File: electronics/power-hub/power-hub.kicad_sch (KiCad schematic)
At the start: 0 parts

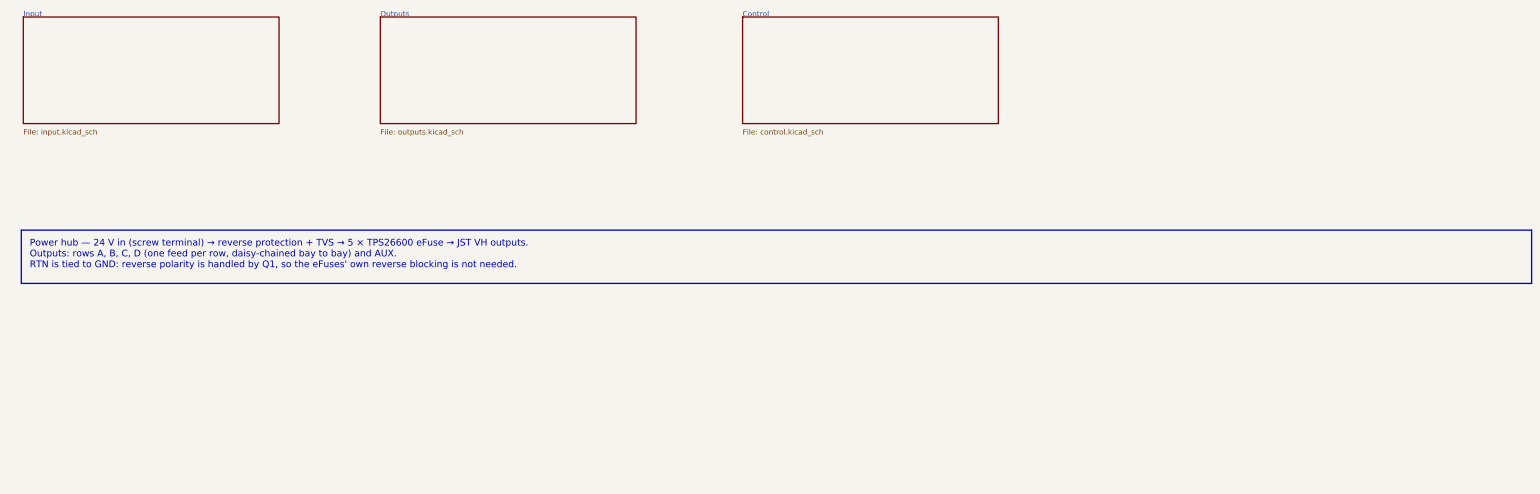
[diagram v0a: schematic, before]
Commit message: Schematics: draw real wires and an overview block diagram
The generator used to connect every pin through a net label only. Now,
in each block, the part with the most pins is the anchor and the
two-pin parts that share a signal with one of its side pins hang off
that pin on a real wire; parts chained behind them (R -> C -> GND)
stack underneath, and anchor-less blocks (pull-ups, reset/boot
buttons) are adopted by the anchor they connect to. Power symbols on
side pins point outward; power-flag references are hidden.

The root sheet becomes a block diagram: the supply rails each sheet
uses across the top, and one lane per pair of sheets listing the
signals they share.

Every wired net still carries one label, so net names, ERC (0) and the
PCB's schematic parity (0) are unchanged; the routed PCBs are untouched.

Co-Authored-By: Claude Opus 5.5 <noreply@anthropic.com>
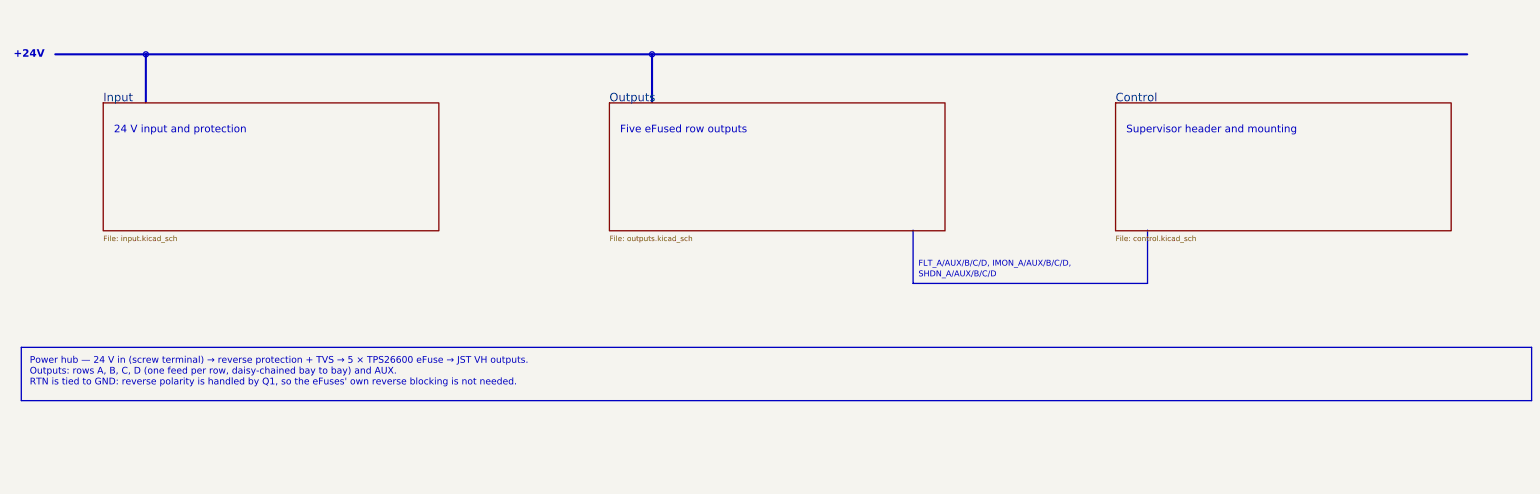
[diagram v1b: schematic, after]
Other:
- note added: "+24V"
- note added: "24 V input and protection"
- note added: "FLT_A/AUX/B/C/D, IMON_A/AUX/B/C/D,"
- note added: "Five eFused row outputs"
- note added: "SHDN_A/AUX/B/C/D"
- note added: "Supervisor header and mounting"
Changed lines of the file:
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@@
 	)
 	(sheet
-		(at 30.48 49.53)
-		(size 60.96 25.4)
+		(at 49.53 70)
+		(size 80 30.48)
 		(exclude_from_sim no)
 		(in_bom yes)
@@
 		(fields_autoplaced yes)
 		(stroke
-			(width 0.1524)
+			(width 0.3)
 			(type solid)
 		)
 		(fill
-			(color 0 0 0 0)
+			(color 255 255 225 1)
 		)
 		(property "Sheetname" "Input"
-			(at 30.48 49.53 0)
-			(effects
-				(font
-					(size 1.27 1.27)
+			(at 49.53 69.85 0)
+			(effects
+				(font
+					(size 2 2)
 				)
 				(justify left bottom)
@@
 		)
 		(property "Sheetfile" "input.kicad_sch"
-			(at 30.48 76.2 0)
+			(at 49.53 101.6 0)
 			(effects
 				(font
@@
 		)
 	)
+	(text "24 V input and protection"
+		(exclude_from_sim no)
+		(at 52.07 77.47 0)
+		(effects
+			(font
+				(size 1.8 1.8)
+			)
+			(justify left bottom)
+		)
+	)
 	(sheet
-		(at 115.57 49.53)
-		(size 60.96 25.4)
+		(at 170.18 70)
+		(size 80 30.48)
 		(exclude_from_sim no)
 		(in_bom yes)
@@
 		(fields_autoplaced yes)
 		(stroke
-			(width 0.1524)
+			(width 0.3)
 			(type solid)
 		)
 		(fill
-			(color 0 0 0 0)
+			(color 255 255 225 1)
 		)
 		(property "Sheetname" "Outputs"
-			(at 115.57 49.53 0)
-			(effects
-				(font
-					(size 1.27 1.27)
+			(at 170.18 69.85 0)
+			(effects
+				(font
+					(size 2 2)
 				)
 				(justify left bottom)
@@
 		)
 		(property "Sheetfile" "outputs.kicad_sch"
-			(at 115.57 76.2 0)
+			(at 170.18 101.6 0)
 			(effects
 				(font
@@
 		)
 	)
+	(text "Five eFused row outputs"
+		(exclude_from_sim no)
+		(at 172.72 77.47 0)
+		(effects
+			(font
+				(size 1.8 1.8)
+			)
+			(justify left bottom)
+		)
+	)
 	(sheet
-		(at 201.93 49.53)
-		(size 60.96 25.4)
+		(at 290.83 70)
+		(size 80 30.48)
 		(exclude_from_sim no)
 		(in_bom yes)
@@
 		(fields_autoplaced yes)
 		(stroke
-			(width 0.1524)
+			(width 0.3)
 			(type solid)
 		)
 		(fill
-			(color 0 0 0 0)
+			(color 255 255 225 1)
 		)
 		(property "Sheetname" "Control"
-			(at 201.93 49.53 0)
-			(effects
-				(font
-					(size 1.27 1.27)
+			(at 290.83 69.85 0)
+			(effects
+				(font
+					(size 2 2)
 				)
 				(justify left bottom)
@@
 		)
 		(property "Sheetfile" "control.kicad_sch"
-			(at 201.93 76.2 0)
+			(at 290.83 101.6 0)
 			(effects
 				(font
@@
 		)
 	)
+	(text "Supervisor header and mounting"
+		(exclude_from_sim no)
+		(at 293.37 77.47 0)
+		(effects
+			(font
+				(size 1.8 1.8)
+			)
+			(justify left bottom)
+		)
+	)
+	(polyline
+		(pts
+			(xy 38.1 58.42)
+			(xy 374.65 58.42)
+		)
+		(stroke
+			(width 0.5)
+			(type default)
+		)
+		(fill
+			(type none)
+		)
+	)
+	(text "+24V"
+		(exclude_from_sim no)
+		(at 35.56 58.42 0)
+		(effects
+			(font
+				(size 1.8 1.8)
+				(bold yes)
+			)
+			(justify right)
+		)
+	)
+	(polyline
+		(pts
+			(xy 59.69 58.42)
+			(xy 59.69 69.85)
+		)
+		(stroke
+			(width 0.5)
+			(type default)
+		)
+		(fill
+			(type none)
+		)
+	)
+	(circle
+		(center 59.69 58.42)
+		(radius 0.6)
+		(stroke
+			(width 0.3)
+			(type default)
+		)
+		(fill
+			(type outline)
+		)
+	)
+	(polyline
+		(pts
+			(xy 180.34 58.42)
+			(xy 180.34 69.85)
+		)
+		(stroke
+			(width 0.5)
+			(type default)
+		)
+		(fill
+			(type none)
+		)
+	)
+	(circle
+		(center 180.34 58.42)
+		(radius 0.6)
+		(stroke
+			(width 0.3)
+			(type default)
+		)
+		(fill
+			(type outline)
+		)
+	)
+	(polyline
+		(pts
+			(xy 242.57 100.33)
+			(xy 242.57 113.03)
+			(xy 298.45 113.03)
+			(xy 298.45 100.33)
+		)
+		(stroke
+			(width 0.3)
+			(type default)
+		)
+		(fill
+			(type none)
+		)
+	)
+	(text "FLT_A/AUX/B/C/D, IMON_A/AUX/B/C/D,"
+		(exclude_from_sim no)
+		(at 243.84 109.22 0)
+		(effects
+			(font
+				(size 1.4 1.4)
+			)
+			(justify left bottom)
+		)
+	)
+	(text "SHDN_A/AUX/B/C/D"
+		(exclude_from_sim no)
+		(at 243.84 111.76 0)
+		(effects
+			(font
+				(size 1.4 1.4)
+			)
+			(justify left bottom)
+		)
+	)
 	(text_box "Power hub — 24 V in (screw terminal) → reverse protection + TVS → 5 × TPS26600 eFuse → JST VH outputs.\nOutputs: rows A, B, C, D (one feed per row, daisy-chained bay to bay) and AUX.\nRTN is tied to GND: reverse polarity is handled by Q1, so the eFuses' own reverse blocking is not needed."
 		(exclude_from_sim no)
-		(at 30 100.33 0)
+		(at 30 128.27 0)
 		(size 360 12.7)
 		(margins 2 2 2 2)

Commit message: Boards v0.2: LMR51635 buck, JST PH, drawn schematics, thermal reliefs
Addresses Fabio's review of v0.1.

Bay node (rev 0.2):
- 5 V buck: LMR51635YDDCR (60 V, 3.5 A, synchronous, 1.1 MHz) with a
  3.3 uH FXL0630, 3 x 22 uF out, 2 x 10 uF + 100 nF in, FB 120k/22k
  (5.16 V), EN 1M/100k UVLO (13.5 V on, 10.8 V off). Replaces the
  TPS54360B, its Schottky and compensation network. CIN straddles the
  VIN/GND pins on solid top-side islands with vias to In1 (TI SLUSF64B).
- 24 V in/out on JST PH (carrier notches resized, rack.yaml pwr_y).
- Power nets named along the path: 24V_BUS -> +24V -> +5V -> DUT_5V_SW
  -> shunt -> DUT_5V; the INA226 visibly runs from +3V3.
- Stackup S+GND / GND / PWR / S+GND: In2 carries +5V, +3V3 under the
  ESP32 and a protected 24 V bus strip. Outer GND pours kept (without
  them Freerouting left ~25 connections unrouted).

Power hub (rev 0.2): JST VH input instead of the screw terminal, JST PH
row outputs, eFuse limit 1.6 A (RILIM 7.5k) to protect the 2 A contacts.

Generator:
- eda.py: drawn schematic mode (sch= placement, Sheet.wire/tag/frame,
  rotated/mirrored symbols, automatic junctions, per-island labels and
  checks that no wire touches another net); all seven sheets redrawn.
- pcbgen.py: thermal reliefs on every pour (+ <board>.kicad_dru for
  single spokes on fine pitch), configurable inner layers, per-zone
  deferral, fixed vias, DRC-driven fix-up for isolated GND pads.
- JLC CPL fix for the LMR51635 (270 deg); BOM, cables, viewer, docs.

ERC 0, DRC 0 copper errors, 0 unconnected, schematic parity 0 on both.

Co-Authored-By: Claude Opus 5.5 <noreply@anthropic.com>
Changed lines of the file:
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@@
 	(title_block
 		(title "Power hub — Overview")
-		(rev "0.1")
+		(rev "0.2")
 		(company "hw-testing-rack")
 		(comment 1 "24 V distribution for the hw-testing-rack shelf: 5 eFused outputs")
@@
 		)
 	)
-	(text_box "Power hub — 24 V in (screw terminal) → reverse protection + TVS → 5 × TPS26600 eFuse → JST VH outputs.\nOutputs: rows A, B, C, D (one feed per row, daisy-chained bay to bay) and AUX.\nRTN is tied to GND: reverse polarity is handled by Q1, so the eFuses' own reverse blocking is not needed."
+	(text_box "Power hub — 24 V in (JST VH) → reverse protection + TVS → 5 × TPS26600 eFuse (1.6 A) → JST PH outputs.\nOutputs: rows A, B, C, D (one feed per row, daisy-chained bay to bay) and AUX.\nRTN is tied to GND: reverse polarity is handled by Q1, so the eFuses' own reverse blocking is not needed."
 		(exclude_from_sim no)
 		(at 30 128.27 0)

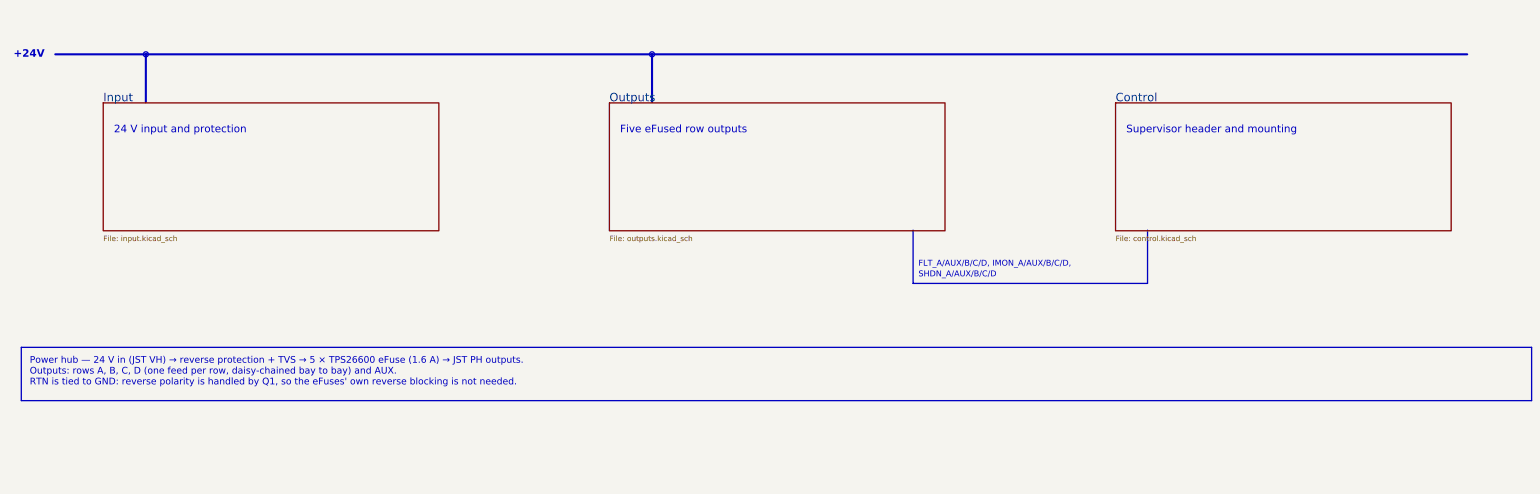
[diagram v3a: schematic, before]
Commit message: Power hub v0.4: eFuses + rack controller (ESP32-S3, CAN master)
A new board for the power box: 76 x 140 mm, 2 layers, drawn around the
outline, holes, row connectors and front LEDs in config/rack.yaml.

- 24 V in on a JST VH (the brick's crimped DC cord), P-FET + TVS + bulk,
  then 4 x TPS26600 (1.6 A) to 6-pin JST PH row outputs: 24 V, GND,
  CAN_H, CAN_L, GND, POS (docs/can.md)
- every row on without firmware (SHDN held high by a 1M/150k divider from
  24 V); the controller can switch a row off (2N7002) and reads FLT and IMON
- rack controller: ESP32-S3-MINI-1, LMR51635 5 V buck (the bay node's
  layout) diode-ORed with USB-C VBUS, AMS1117; TCAN1044AV with both
  terminations of the star bus (2 x 56 ohm split, twice), PESD2CAN; POS per
  row through 10k + BAT54S clamp (survives a reversed cable)
- side-view ON / FAULT LEDs per row, 24V and CTL in the box's front wall
- autorouted; ERC 0, DRC 0, 0 unconnected, parity 0; Konnect review in
  docs/review-konnect.md (VBUS cap added; the rest per-sheet false positives)
- box re-generated for the final hole / connector / LED positions; viewer
  shows the real board; BOM carries an estimate (Standard PCBA, not quoted)
- schematic: automatic block layout for now

Co-Authored-By: Claude Opus 5.5 <noreply@anthropic.com>
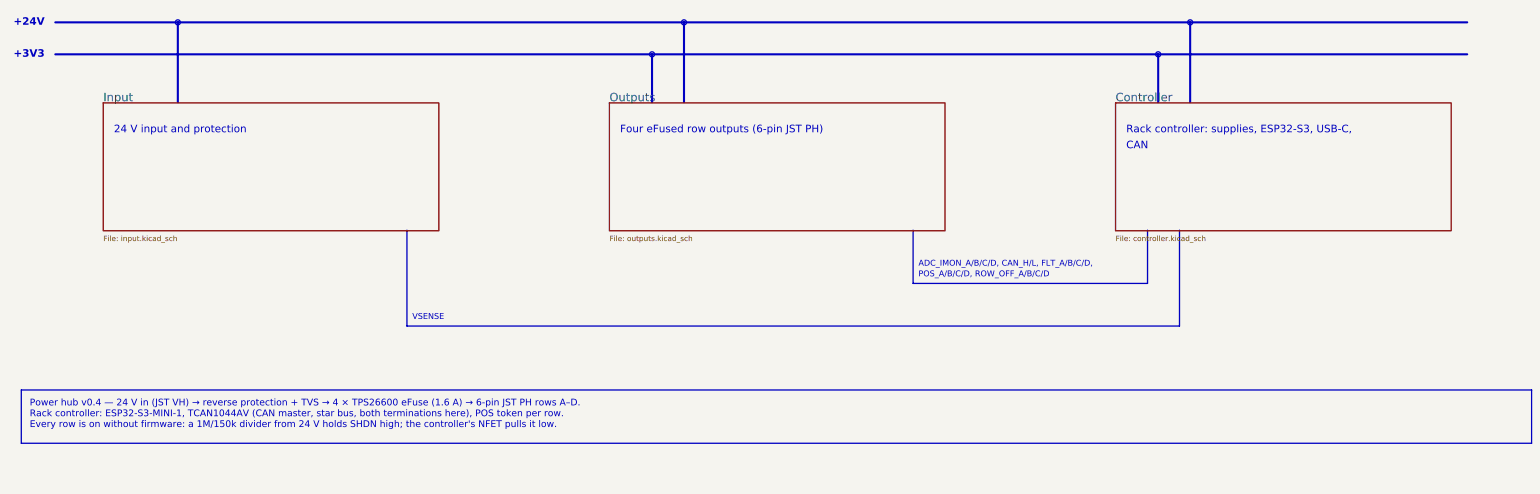
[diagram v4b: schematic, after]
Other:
- removed sheet Control
- added sheet Controller (controller.kicad_sch)
- note added: "+3V3"
- note added: "ADC_IMON_A/B/C/D, CAN_H/L, FLT_A/B/C/D,"
- note added: "CAN"
- note added: "Four eFused row outputs (6-pin JST PH)"
- note added: "POS_A/B/C/D, ROW_OFF_A/B/C/D"
- note added: "Rack controller: supplies, ESP32-S3, USB-C,"
- note added: "VSENSE"
- note removed: "FLT_A/AUX/B/C/D, IMON_A/AUX/B/C/D,"
- note removed: "Five eFused row outputs"
- note removed: "SHDN_A/AUX/B/C/D"
- note removed: "Supervisor header and mounting"
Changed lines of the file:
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@@
 	(title_block
 		(title "Power hub — Overview")
-		(rev "0.3")
+		(rev "0.4")
 		(company "hw-testing-rack")
-		(comment 1 "24 V distribution for the hw-testing-rack shelf: 5 eFused outputs")
+		(comment 1 "24 V distribution + rack controller (ESP32-S3, CAN master) for the hw-testing-rack")
 		(comment 2 "Generated from electronics/power-hub/design.py — edit the Python, then regenerate")
 	)
@@
 		)
 	)
-	(text "Five eFused row outputs"
+	(text "Four eFused row outputs (6-pin JST PH)"
 		(exclude_from_sim no)
 		(at 172.72 77.47 0)
@@
 			(color 255 255 225 1)
 		)
-		(property "Sheetname" "Control"
+		(property "Sheetname" "Controller"
 			(at 290.83 69.85 0)
 			(effects
@@
 			)
 		)
-		(property "Sheetfile" "control.kicad_sch"
+		(property "Sheetfile" "controller.kicad_sch"
 			(at 290.83 101.6 0)
 			(effects
@@
 		)
 	)
-	(text "Supervisor header and mounting"
+	(text "Rack controller: supplies, ESP32-S3, USB-C,"
 		(exclude_from_sim no)
 		(at 293.37 77.47 0)
+		(effects
+			(font
+				(size 1.8 1.8)
+			)
+			(justify left bottom)
+		)
+	)
+	(text "CAN"
+		(exclude_from_sim no)
+		(at 293.37 81.28 0)
 		(effects
 			(font
@@
 		)
 	)
-	(text "+24V"
+	(text "+3V3"
 		(exclude_from_sim no)
 		(at 35.56 58.42 0)
@@
 			)
 			(justify right)
-		)
-	)
-	(polyline
-		(pts
-			(xy 59.69 58.42)
-			(xy 59.69 69.85)
-		)
-		(stroke
-			(width 0.5)
-			(type default)
-		)
-		(fill
-			(type none)
-		)
-	)
-	(circle
-		(center 59.69 58.42)
-		(radius 0.6)
-		(stroke
-			(width 0.3)
-			(type default)
-		)
-		(fill
-			(type outline)
 		)
 	)
@@
 	(circle
 		(center 180.34 58.42)
+		(radius 0.6)
+		(stroke
+			(width 0.3)
+			(type default)
+		)
+		(fill
+			(type outline)
+		)
+	)
+	(polyline
+		(pts
+			(xy 300.99 58.42)
+			(xy 300.99 69.85)
+		)
+		(stroke
+			(width 0.5)
+			(type default)
+		)
+		(fill
+			(type none)
+		)
+	)
+	(circle
+		(center 300.99 58.42)
+		(radius 0.6)
+		(stroke
+			(width 0.3)
+			(type default)
+		)
+		(fill
+			(type outline)
+		)
+	)
+	(polyline
+		(pts
+			(xy 38.1 50.8)
+			(xy 374.65 50.8)
+		)
+		(stroke
+			(width 0.5)
+			(type default)
+		)
+		(fill
+			(type none)
+		)
+	)
+	(text "+24V"
+		(exclude_from_sim no)
+		(at 35.56 50.8 0)
+		(effects
+			(font
+				(size 1.8 1.8)
+				(bold yes)
+			)
+			(justify right)
+		)
+	)
+	(polyline
+		(pts
+			(xy 67.31 50.8)
+			(xy 67.31 69.85)
+		)
+		(stroke
+			(width 0.5)
+			(type default)
+		)
+		(fill
+			(type none)
+		)
+	)
+	(circle
+		(center 67.31 50.8)
+		(radius 0.6)
+		(stroke
+			(width 0.3)
+			(type default)
+		)
+		(fill
+			(type outline)
+		)
+	)
+	(polyline
+		(pts
+			(xy 187.96 50.8)
+			(xy 187.96 69.85)
+		)
+		(stroke
+			(width 0.5)
+			(type default)
+		)
+		(fill
+			(type none)
+		)
+	)
+	(circle
+		(center 187.96 50.8)
+		(radius 0.6)
+		(stroke
+			(width 0.3)
+			(type default)
+		)
+		(fill
+			(type outline)
+		)
+	)
+	(polyline
+		(pts
+			(xy 308.61 50.8)
+			(xy 308.61 69.85)
+		)
+		(stroke
+			(width 0.5)
+			(type default)
+		)
+		(fill
+			(type none)
+		)
+	)
+	(circle
+		(center 308.61 50.8)
 		(radius 0.6)
 		(stroke
@@
 		)
 	)
-	(text "FLT_A/AUX/B/C/D, IMON_A/AUX/B/C/D,"
+	(text "ADC_IMON_A/B/C/D, CAN_H/L, FLT_A/B/C/D,"
 		(exclude_from_sim no)
 		(at 243.84 109.22 0)
@@
 		)
 	)
-	(text "SHDN_A/AUX/B/C/D"
+	(text "POS_A/B/C/D, ROW_OFF_A/B/C/D"
 		(exclude_from_sim no)
 		(at 243.84 111.76 0)
@@
 		)
 	)
-	(text_box "Power hub — 24 V in (JST VH) → reverse protection + TVS → 5 × TPS26600 eFuse (1.6 A) → JST PH outputs.\nOutputs: rows A, B, C, D (one feed per row, daisy-chained bay to bay) and AUX.\nRTN is tied to GND: reverse polarity is handled by Q1, so the eFuses' own reverse blocking is not needed."
-		(exclude_from_sim no)
-		(at 30 128.27 0)
+	(polyline
+		(pts
+			(xy 121.92 100.33)
+			(xy 121.92 123.19)
+			(xy 306.07 123.19)
+			(xy 306.07 100.33)
+		)
+		(stroke
+			(width 0.3)
+			(type default)
+		)
+		(fill
+			(type none)
+		)
+	)
+	(text "VSENSE"
+		(exclude_from_sim no)
+		(at 123.19 121.92 0)
+		(effects
+			(font
+				(size 1.4 1.4)
+			)
+			(justify left bottom)
+		)
+	)
+	(text_box "Power hub v0.4 — 24 V in (JST VH) → reverse protection + TVS → 4 × TPS26600 eFuse (1.6 A) → 6-pin JST PH rows A–D.\nRack controller: ESP32-S3-MINI-1, TCAN1044AV (CAN master, star bus, both terminations here), POS token per row.\nEvery row is on without firmware: a 1M/150k divider from 24 V holds SHDN high; the controller's NFET pulls it low."
+		(exclude_from_sim no)
+		(at 30 138.43 0)
 		(size 360 12.7)
 		(margins 2 2 2 2)
